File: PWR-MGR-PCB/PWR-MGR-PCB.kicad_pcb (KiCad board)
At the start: 2 copper layers, 32 x 37.4 mm, 23 parts, among them J1 USB_C_Receptacle_USB2.0_16P, J2 Battery_1x2, J3 Conn_01x01_Pin, J4 Conn_01x01_Pin, J5 Conn_01x01_Pin, J6 Conn_01x01_Pin, U1 USBLC6-2SC6, U2 TLV75533PDBV, U3 BQ24074RGT

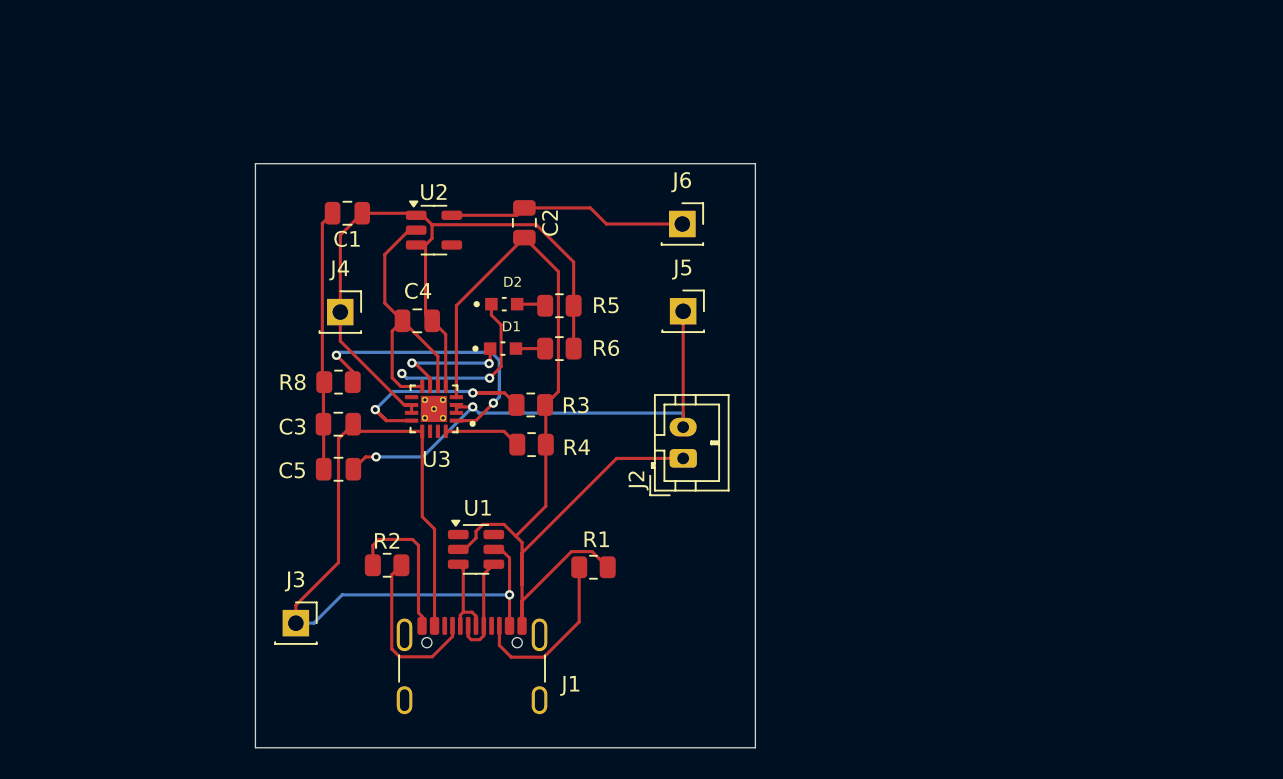
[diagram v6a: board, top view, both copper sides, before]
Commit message: Update diode component
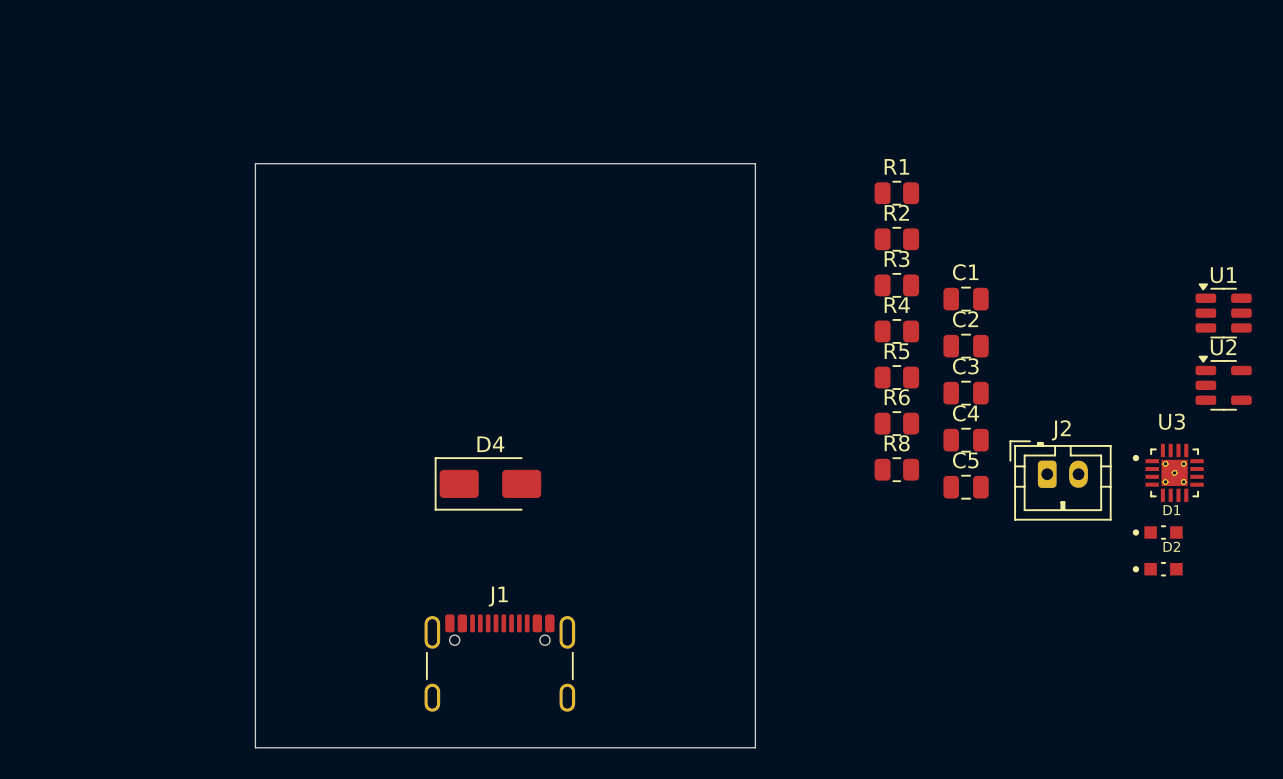
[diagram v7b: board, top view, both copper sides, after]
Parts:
- removed J3, J4, J5, J6: Conn_01x01_Pin, Connector_PinSocket_2.54mm:PinSocket_1x01_P2.54mm_Vertical
- added D4: SS34, Diode_SMD:D_SMA, F.Cu at (156.4, 94.9)
- J1: value USB_C_Receptacle_USB2.0_16P -> USB_C_Receptacle_USB2.0_14P
- moved U2 51.5 mm to (203.3, 88.6)
- moved U1 50.2 mm to (203.3, 83.9)
- moved U3 47.6 mm to (200.2, 94.2), turned to 0 degrees
- moved D2 45.5 mm to (199.5, 100.3)
- moved D1 43.9 mm to (199.5, 98.0)
- moved C3 40.2 mm to (186.8, 89.1), turned to 0 degrees
- moved C5 40.2 mm to (186.8, 95.1), turned to 0 degrees
- moved C1 40.0 mm to (186.8, 83.0), turned to 0 degrees
- moved R2 38.7 mm to (182.4, 79.2), turned to 0 degrees
- moved R8 36.2 mm to (182.4, 94.0), turned to 0 degrees
- moved C4 35.9 mm to (186.8, 92.1), turned to 0 degrees
- moved R1 30.8 mm to (182.4, 76.3)
- moved C2 29.4 mm to (186.8, 86.0), turned to 0 degrees
- moved R3 24.7 mm to (182.4, 82.2), turned to 0 degrees
- moved R4 24.5 mm to (182.4, 85.1), turned to 0 degrees
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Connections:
- net /VBATT_TEST renamed /V_BATT
- J1 pad A4: VBUS 5V -> Net-(D4-A)
- J1 pad A8: unconnected-(J1-SBU1-PadA8) -> (no net)
- J1 pad A9: VBUS 5V -> Net-(D4-A)
- J1 pad B4: VBUS 5V -> Net-(D4-A)
- J1 pad B8: unconnected-(J1-SBU2-PadB8) -> (no net)
- J1 pad B9: VBUS 5V -> Net-(D4-A)
- J1 pad S1: unconnected-(J1-SHIELD-PadS1) -> GND
- U1 pad 1: unconnected-(U1-I/O1-Pad1) -> /USB_CONN_D+
- U1 pad 4: /USB_CONN_D+ -> D-
- U1 pad 6: unconnected-(U1-I/O1-Pad6) -> D+
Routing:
- net GND: track 113.3 -> 0.00 mm
- net VBUS 5V: track 52.2 -> 0.00 mm, vias 1 -> 0
- net VCC_BMS: track 47.5 -> 0.00 mm
- net /V_BATT: track 33.6 -> 0.00 mm, vias 2 -> 0
- net Net-(U3-TS): track 18.6 -> 0.00 mm, vias 2 -> 0
- net Net-(U3-ILIM): track 18.0 -> 0.00 mm, vias 2 -> 0
- net +3.3V: track 15.4 -> 0.00 mm
- net Net-(J1-CC2): track 11.1 -> 0.00 mm
- net Net-(U3-~{CHG}): track 11.0 -> 0.00 mm, vias 2 -> 0
- net Net-(J1-CC1): track 10.9 -> 0.00 mm
- net Net-(U3-~{PGOOD}): track 8.51 -> 0.00 mm, vias 2 -> 0
- net /USB_CONN_D+: track 6.71 -> 0.00 mm
- net /USB_CONN_D-: track 5.70 -> 0.00 mm
- net Net-(U3-ISET): track 5.54 -> 0.00 mm
- net Net-(D2-PadA): track 1.91 -> 0.00 mm
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
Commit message: Begin placing board
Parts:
- moved U2 54.9 mm to (148.6, 83.9)
- moved U1 46.3 mm to (157.4, 89.8)
- moved R1 40.2 mm to (149.6, 99.6)
- moved U3 36.2 mm to (165.2, 84.5)
- moved R2 26.8 mm to (164.9, 99.6)
- moved D4 2.39 mm to (157.4, 97.0)
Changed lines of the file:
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@@
 	(footprint "Resistor_SMD:R_0805_2012Metric"
 		(layer "F.Cu")
-		(at 182.384 79.21)
+		(at 164.9495 99.568)
 		(descr "Resistor SMD 0805 (2012 Metric), square (rectangular) end terminal, IPC-7351 nominal, (Body size source: IPC-SM-782 page 72, https://www.pcb-3d.com/wordpress/wp-content/uploads/ipc-sm-782a_amendment_1_and_2.pdf), generated with kicad-footprint-generator")
 		(tags "resistor")
@@
 	(footprint "BQ24074RGTR:QFN50P300X300X100-17N"
 		(layer "F.Cu")
-		(at 200.164 94.165)
+		(at 165.239 84.493)
 		(property "Reference" "U3"
 			(at -0.165 -3.24 0)
@@
 	(footprint "Package_TO_SOT_SMD:SOT-23-5"
 		(layer "F.Cu")
-		(at 203.304 88.56)
+		(at 148.5955 83.881)
 		(descr "SOT, 5 Pin (JEDEC MO-178 Var AA https://www.jedec.org/document_search?search_api_views_fulltext=MO-178), generated with kicad-footprint-generator ipc_gullwing_generator.py")
 		(tags "SOT TO_SOT_SMD")
@@
 	(footprint "Resistor_SMD:R_0805_2012Metric"
 		(layer "F.Cu")
-		(at 182.384 76.26)
+		(at 149.5825 99.568)
 		(descr "Resistor SMD 0805 (2012 Metric), square (rectangular) end terminal, IPC-7351 nominal, (Body size source: IPC-SM-782 page 72, https://www.pcb-3d.com/wordpress/wp-content/uploads/ipc-sm-782a_amendment_1_and_2.pdf), generated with kicad-footprint-generator")
 		(tags "resistor")
@@
 	(footprint "Package_TO_SOT_SMD:SOT-23-6"
 		(layer "F.Cu")
-		(at 203.304 83.935)
+		(at 157.3585 89.85)
 		(descr "SOT, 6 Pin (JEDEC MO-178 Var AB https://www.jedec.org/document_search?search_api_views_fulltext=MO-178), generated with kicad-footprint-generator ipc_gullwing_generator.py")
 		(tags "SOT TO_SOT_SMD")
@@
 	(footprint "Diode_SMD:D_SMA"
 		(layer "F.Cu")
-		(at 156.369 94.869)
+		(at 157.385 97.028)
 		(descr "Diode SMA (DO-214AC)")
 		(tags "Diode SMA (DO-214AC)")
